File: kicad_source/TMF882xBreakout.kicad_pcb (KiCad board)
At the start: 2 copper layers, 28 x 20 mm, 27 parts, among them CN1 CONN_01X06, CN2 CONN_01X07, CN3 SM05B-SRSS-TB, CN4 SM05B-SRSS-TB, Q1 BSS138, Q2 BSS138, Q3 BSS138, U1 MIC5225-3.3, U2 TMF8801

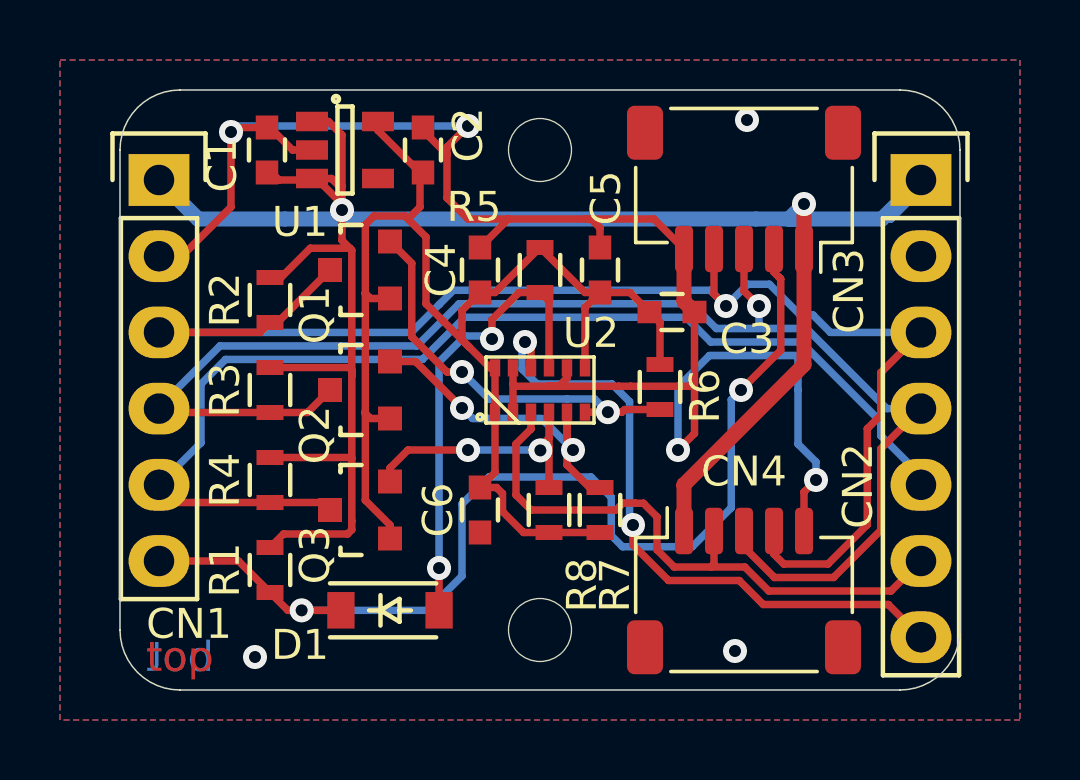
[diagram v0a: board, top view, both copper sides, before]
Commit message: updated project, added footprint for TMF882x
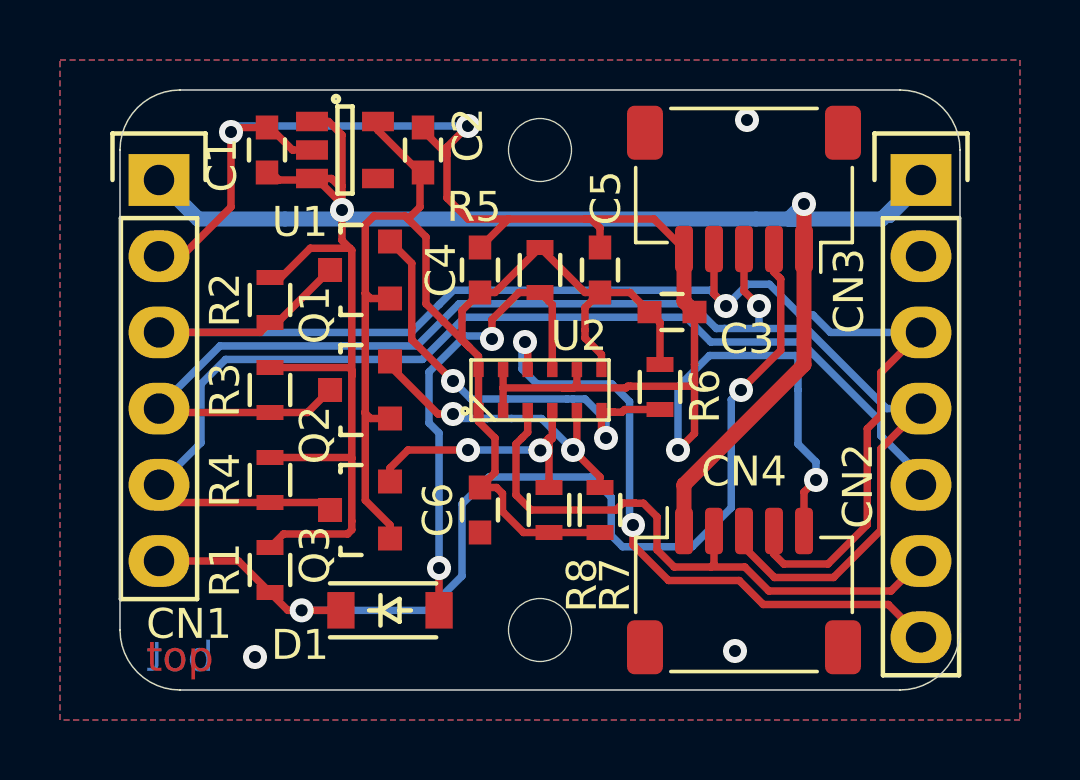
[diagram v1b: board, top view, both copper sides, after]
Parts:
- U2: value TMF8801 -> TMF882x; footprint IC_sensor:TMF8801 -> IC_sensor:TMF882x
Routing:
- net /I2C_SCL: track 12.0 -> 10.6 mm
- net /I2C_SDA: track 13.6 -> 15.0 mm
- net /INT: track 8.84 -> 9.48 mm
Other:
- board text added: "TMF882x Breakout 0.1"
- board text removed: "TMF8801 Breakout 0.1"
